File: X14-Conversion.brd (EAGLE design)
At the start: 160 x 100 mm, 34 parts, among them U2 LM2678

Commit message: Added conversion board library
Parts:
- removed +12V, +3.3, 5V, 5V_3.3_TP, GND_TP: TP, TP:TP
- removed +3.3V, +5V, 12V, 5V_3.3, GND, GND3: (no value), SparkFun-Connectors:BANANA_CONN
- removed C14, C29, C30, C31: 10uF, PowerComponents:CTAN(7.30_4.30MM)
- removed C20: 10nF, SparkFun-Capacitors:0603
- removed C24, C25, C26: 150uF, PowerComponents:CTAN(7.30_4.30MM)
- removed C3: 0.47uF, rcl:C0603
- removed D2, D3, D4: (no value), SparkFun-LED:LED-0603
- removed R1, R2, R3, R5: 470, SparkFun-Resistors:0603
- removed R4: 1.2 ohms, SparkFun-Resistors:0603
- removed U$13: 47 uF, Nordic_nRF:RESC0603_N
- removed U$3: SWITCHMODE_SCHOTTKY, PowerComponents:DPAK-3
- removed U$4: TO-263, TPS758:TO-263
- removed U$7: HCM1305, HCM1305:HCM1305
- removed U2: LM2678, PowerComponents:LM2678
- added CB: 10nF 0Ohm, CGA4C2C0G1H103J060AA:CAP_2012_TDK
- added CIN: 120uF 25mOhm, 20SVPF120M:PCAP_SVP_C6_PAN
- added CINX: 100nF 1mOhm, GRM155R71C104KA88D:CAP_GRM_155_MUR
- added COUT: 180uF 30mOhm, 16SVP180MX:CAP_16SVP180MX
- added L1: 15uH 28.5mOhm, IND, 15uH - hcma1305:HCMA1305
- added RFB1: 1kOhm, CRCW04021K00FKED:RES_CRCW_0402
- added RFB2: 3.32kOhm, CRCW04023K32FKED:RES_CRCW_0402
- added U1: LM2678, LM2678SX-ADJNOPB:TS7B
- D1: value (none) -> 550mV 5A; device SparkFun-LED:LED-0603 -> CDBC520-G_Library:CDBC-G
- moved D1 205.8 mm to (-25.4, -5.08)
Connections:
- removed net +12V: +12V.P$1, 12V.P$1, C14.+, C29.+, C3.1, C30.+, C31.+, R5.2, U2.2
- removed net +3.3V: +3.3.P$1, +3.3V.P$1, R3.2, U$13.1, U$4.P$4
- removed net +5V: +5V.P$1, 5V.P$1, R2.2
- removed net +5V_3.3V: 5V_3.3.P$1, 5V_3.3_TP.P$1, C24.+, C25.+, C26.+, R1.2, U$4.P$1, U$4.P$2, U$7.2, U2.6
- removed net GND: C14.-, C24.-, C25.-, C26.-, C29.-, C3.2, C30.-, C31.-, D1.C, D2.C, D3.C, D4.C, GND.P$1, GND3.P$1, GND_TP.P$1, R4.1, U$3.P$1, U$3.P$3, U$4.P$3, U$4.P$6, U2.4, U2.TAB
- removed net N$10: R4.2, U$13.2
- removed net N$2: C20.1, U2.3
- removed net N$4: D2.A, R5.1
- removed net N$5: D3.A, R3.1
- removed net N$6: D4.A, R1.1
- removed net N$7: C20.2, U$3.P$4, U$7.1, U2.1
- removed net N$8: D1.A, R2.1

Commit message: Update new parts library
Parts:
- CB: value 10nF 0Ohm -> 10nF 0Ω
- CIN: value 120uF 25mOhm -> 120uF 25mΩ
- CINX: value 100nF 1mOhm -> 100nF 1mΩ
- COUT: value 180uF 30mOhm -> 180uF 30mΩ
- L1: value 15uH 28.5mOhm -> 15uH
- RFB1: value 1kOhm -> 1kΩ
- RFB2: value 3.32kOhm -> 3.32kΩ
- moved U1 102.9 mm to (-78.7, -71.1)
- moved RFB1 63.8 mm to (-53.3, -41.9)
- moved CIN 61.2 mm to (-52.1, -54.6)
- moved D1 49.7 mm to (-52.1, -47.0)
- moved CB 48.6 mm to (-53.3, -77.5)
- moved CINX 48.6 mm to (-68.6, -80.0)
- moved L1 48.6 mm to (-49.5, -68.6)
- moved RFB2 48.6 mm to (-53.3, -59.7)
- moved COUT 48.6 mm to (-66.0, -69.8)
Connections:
- new net GND: RFB1.1
- new net N$1: RFB1.2, RFB2.2, U1.6

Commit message: Complete Schematic for LM2678
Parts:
- U1: value LM2678 -> LM2678SX-ADJ/NOPBTS7B
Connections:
- new net 12V: CIN.1, CINX.1, U1.2
- new net 5V: COUT.1, L1.2, RFB2.1
- new net N$2: CB.1, U1.3
- new net N$3: CB.2, D1.1, L1.1, U1.1
- net GND: now also CIN.2, CINX.2, COUT.2, D1.2, U1.4
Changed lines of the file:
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@@
 <attribute name="VALUE" x="-70.3088" y="-80.645" size="1.27" layer="27" ratio="6"/>
 </element>
-<element name="U1" library="LM2678SX-ADJNOPB" package="TS7B" value="LM2678" x="-78.74" y="-71.12" smashed="yes">
+<element name="U1" library="LM2678SX-ADJNOPB" package="TS7B" value="LM2678SX-ADJ/NOPBTS7B" x="-78.74" y="-71.12" smashed="yes">
 <attribute name="COPYRIGHT" value="Copyright (C) 2021 Ultra Librarian. All rights reserved." x="-78.74" y="-71.12" size="1.778" layer="27" display="off"/>
 <attribute name="DIGI-KEY_PART_NUMBER_1" value="LM2678SX-ADJ/NOPBCT-ND" x="-78.74" y="-71.12" size="1.778" layer="27" display="off"/>
@@
 </elements>
 <signals>
-<signal name="GND">
-<contactref element="RFB1" pad="1"/>
-</signal>
 <signal name="N$1">
 <contactref element="U1" pad="6"/>
@@
 <wire x1="-52.8701" y1="-41.91" x2="-52.8701" y2="-59.69" width="0" layer="19" extent="1-1"/>
 </signal>
+<signal name="GND">
+<contactref element="RFB1" pad="1"/>
+<contactref element="COUT" pad="2"/>
+<contactref element="D1" pad="2"/>
+<contactref element="CIN" pad="2"/>
+<contactref element="CINX" pad="2"/>
+<contactref element="U1" pad="4"/>
+<wire x1="-68.0593" y1="-80.01" x2="-78.74" y2="-79.4004" width="0" layer="19" extent="1-1"/>
+<wire x1="-61.69" y1="-69.85" x2="-68.0593" y2="-80.01" width="0" layer="19" extent="1-1"/>
+<wire x1="-49.3141" y1="-54.61" x2="-61.69" y2="-69.85" width="0" layer="19" extent="1-1"/>
+<wire x1="-48.943" y1="-46.99" x2="-49.3141" y2="-54.61" width="0" layer="19" extent="1-1"/>
+<wire x1="-53.8099" y1="-41.91" x2="-48.943" y2="-46.99" width="0" layer="19" extent="1-1"/>
+</signal>
+<signal name="N$2">
+<contactref element="U1" pad="3"/>
+<contactref element="CB" pad="1"/>
+<wire x1="-54.5211" y1="-77.47" x2="-80.01" y2="-79.4004" width="0" layer="19" extent="1-1"/>
+</signal>
+<signal name="N$3">
+<contactref element="U1" pad="1"/>
+<contactref element="L1" pad="1"/>
+<contactref element="CB" pad="2"/>
+<contactref element="D1" pad="1"/>
+<wire x1="-55.13" y1="-68.58" x2="-82.55" y2="-79.4004" width="0" layer="19" extent="1-1"/>
+<wire x1="-52.1589" y1="-77.47" x2="-55.13" y2="-68.58" width="0" layer="19" extent="1-1"/>
+<wire x1="-55.197" y1="-46.99" x2="-55.13" y2="-68.58" width="0" layer="19" extent="1-1"/>
+</signal>
+<signal name="12V">
+<contactref element="U1" pad="2"/>
+<contactref element="CIN" pad="1"/>
+<contactref element="CINX" pad="1"/>
+<wire x1="-69.1007" y1="-80.01" x2="-81.28" y2="-79.4004" width="0" layer="19" extent="1-1"/>
+<wire x1="-54.8259" y1="-54.61" x2="-69.1007" y2="-80.01" width="0" layer="19" extent="1-1"/>
+</signal>
+<signal name="5V">
+<contactref element="L1" pad="2"/>
+<contactref element="COUT" pad="1"/>
+<contactref element="RFB2" pad="1"/>
+<wire x1="-53.8099" y1="-59.69" x2="-70.39" y2="-69.85" width="0" layer="19" extent="1-1"/>
+<wire x1="-43.93" y1="-68.58" x2="-53.8099" y2="-59.69" width="0" layer="19" extent="1-1"/>
+</signal>
 </signals>

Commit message: Fix Schematic
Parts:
- added C1: 10uF 16V, CAP_GRM21BR61C106KE15L:CAPC2012X135N
- added C2: 22uF 16V, CAP_GRM21BR61C226ME44L:CAPC2012X145N
- added U$1: SOT150P410X160-3N, AZ1117C-3.3:SOT150P410X160-3N
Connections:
- new net 3.3V: C1.1, U$1.2
- net 5V: now also C2.1, U$1.3
- net GND: now also C1.2, C2.2, U$1.1
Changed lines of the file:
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@@
 <attribute name="VALUE" x="-80.4688" y="-71.755" size="1.27" layer="27" ratio="6"/>
+</element>
+<element name="U$1" library="AZ1117C-3.3" package="SOT150P410X160-3N" value="SOT150P410X160-3N" x="-74.93" y="-90.17" smashed="yes">
+<attribute name="NAME" x="-82.601959375" y="-85.967259375" size="3.2051" layer="25" display="off"/>
+<attribute name="VALUE" x="-83.074790625" y="-95.6813" size="1.27" layer="27"/>
+</element>
+<element name="C1" library="CAP_GRM21BR61C106KE15L" package="CAPC2012X135N" value="10uF 16V" x="-82.55" y="-99.06" smashed="yes">
+<attribute name="DESCRIPTION" value=" 10 µF ±10% 16V Ceramic Capacitor X5R 0805 (2012 Metric) " x="-82.55" y="-99.06" size="1.778" layer="27" display="off"/>
+<attribute name="DIGI-KEY_PART_NUMBER" value="490-3886-2-ND" x="-82.55" y="-99.06" size="1.778" layer="27" display="off"/>
+<attribute name="MF" value="Murata" x="-82.55" y="-99.06" size="1.778" layer="27" display="off"/>
+<attribute name="MP" value="GRM21BR61C106KE15L" x="-82.55" y="-99.06" size="1.778" layer="27" display="off"/>
+<attribute name="NAME" x="-84.21" y="-98.04" size="0.5" layer="25"/>
+<attribute name="PACKAGE" value="2012 Murata" x="-82.55" y="-99.06" size="1.778" layer="27" display="off"/>
+<attribute name="PURCHASE-URL" value="https://pricing.snapeda.com/search/part/GRM21BR61C106KE15L/?ref=eda" x="-82.55" y="-99.06" size="1.778" layer="27" display="off"/>
+<attribute name="VALUE" x="-84.21" y="-100.08" size="0.5" layer="27" align="top-left"/>
+</element>
+<element name="C2" library="CAP_GRM21BR61C226ME44L" package="CAPC2012X145N" value="22uF 16V" x="-82.55" y="-102.87" smashed="yes">
+<attribute name="DESCRIPTION" value=" SMD Capacitor X5R(EIA) with Capacitance: 22uF Tol. 20%. Rated Voltage: 16Vdc " x="-82.55" y="-102.87" size="1.778" layer="27" display="off"/>
+<attribute name="DIGI-KEY_PART_NUMBER" value="490-10747-2-ND" x="-82.55" y="-102.87" size="1.778" layer="27" display="off"/>
+<attribute name="MF" value="Murata" x="-82.55" y="-102.87" size="1.778" layer="27" display="off"/>
+<attribute name="MP" value="GRM21BR61C226ME44L" x="-82.55" y="-102.87" size="1.778" layer="27" display="off"/>
+<attribute name="NAME" x="-84.26" y="-101.8" size="0.5" layer="25"/>
+<attribute name="PACKAGE" value="2012 Murata" x="-82.55" y="-102.87" size="1.778" layer="27" display="off"/>
+<attribute name="PURCHASE-URL" value="https://pricing.snapeda.com/search/part/GRM21BR61C226ME44L/?ref=eda" x="-82.55" y="-102.87" size="1.778" layer="27" display="off"/>
+<attribute name="VALUE" x="-84.26" y="-103.94" size="0.5" layer="27" align="top-left"/>
 </element>
 </elements>
@@
 <contactref element="CINX" pad="2"/>
 <contactref element="U1" pad="4"/>
+<contactref element="C2" pad="2"/>
+<contactref element="U$1" pad="1"/>
+<contactref element="C1" pad="2"/>
+<wire x1="-81.662" y1="-99.06" x2="-81.65" y2="-102.87" width="0" layer="19" extent="1-1"/>
+<wire x1="-76.429" y1="-92.151" x2="-81.662" y2="-99.06" width="0" layer="19" extent="1-1"/>
+<wire x1="-78.74" y1="-79.4004" x2="-76.429" y2="-92.151" width="0" layer="19" extent="1-1"/>
 <wire x1="-68.0593" y1="-80.01" x2="-78.74" y2="-79.4004" width="0" layer="19" extent="1-1"/>
 <wire x1="-61.69" y1="-69.85" x2="-68.0593" y2="-80.01" width="0" layer="19" extent="1-1"/>
@@
 <contactref element="COUT" pad="1"/>
 <contactref element="RFB2" pad="1"/>
+<contactref element="U$1" pad="3"/>
+<contactref element="C2" pad="1"/>
+<wire x1="-73.431" y1="-92.151" x2="-83.45" y2="-102.87" width="0" layer="19" extent="1-1"/>
+<wire x1="-70.39" y1="-69.85" x2="-73.431" y2="-92.151" width="0" layer="19" extent="1-1"/>
 <wire x1="-53.8099" y1="-59.69" x2="-70.39" y2="-69.85" width="0" layer="19" extent="1-1"/>
 <wire x1="-43.93" y1="-68.58" x2="-53.8099" y2="-59.69" width="0" layer="19" extent="1-1"/>
 </signal>
+<signal name="3.3V">
+<contactref element="U$1" pad="2"/>
+<contactref element="C1" pad="1"/>
+<wire x1="-74.93" y1="-91.897" x2="-83.438" y2="-99.06" width="0" layer="19" extent="1-1"/>
+</signal>
 </signals>

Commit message: Completing Schematic
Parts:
- added CONN: DISTRIBUTION-CONVERSION, CONN, Distribution-Conversion:TSW-105-05-G-S
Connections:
- new net 5.2V: C2.1, COUT.1, L1.2, RFB2.1, U$1.3
- net 12V: now also CONN.1
- net 3.3V: now also CONN.2
- net 5V: now also CONN.3; no longer C2.1, COUT.1, L1.2, RFB2.1, U$1.3
- net GND: now also CONN.4, CONN.5
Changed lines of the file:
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@@
 <attribute name="VALUE" x="-84.26" y="-103.94" size="0.5" layer="27" align="top-left"/>
+</element>
+<element name="CONN" library="CONN, Distribution-Conversion" package="TSW-105-05-G-S" value="DISTRIBUTION-CONVERSION" x="-77.47" y="-109.22" smashed="yes">
+<attribute name="NAME" x="-83.82" y="-107.95" size="1.778" layer="25"/>
 </element>
 </elements>
@@
 <contactref element="U$1" pad="1"/>
 <contactref element="C1" pad="2"/>
+<contactref element="CONN" pad="5"/>
+<contactref element="CONN" pad="4"/>
 <wire x1="-81.662" y1="-99.06" x2="-81.65" y2="-102.87" width="0" layer="19" extent="1-1"/>
 <wire x1="-76.429" y1="-92.151" x2="-81.662" y2="-99.06" width="0" layer="19" extent="1-1"/>
+<wire x1="-74.95" y1="-109.22" x2="-81.65" y2="-102.87" width="0" layer="19" extent="1-1"/>
+<wire x1="-72.41" y1="-109.22" x2="-74.95" y2="-109.22" width="0" layer="19" extent="1-1"/>
 <wire x1="-78.74" y1="-79.4004" x2="-76.429" y2="-92.151" width="0" layer="19" extent="1-1"/>
 <wire x1="-68.0593" y1="-80.01" x2="-78.74" y2="-79.4004" width="0" layer="19" extent="1-1"/>
@@
 <wire x1="-55.197" y1="-46.99" x2="-55.13" y2="-68.58" width="0" layer="19" extent="1-1"/>
 </signal>
-<signal name="12V">
-<contactref element="U1" pad="2"/>
-<contactref element="CIN" pad="1"/>
-<contactref element="CINX" pad="1"/>
-<wire x1="-69.1007" y1="-80.01" x2="-81.28" y2="-79.4004" width="0" layer="19" extent="1-1"/>
-<wire x1="-54.8259" y1="-54.61" x2="-69.1007" y2="-80.01" width="0" layer="19" extent="1-1"/>
+<signal name="5V">
+<contactref element="CONN" pad="3"/>
 </signal>
-<signal name="5V">
+<signal name="3.3V">
+<contactref element="U$1" pad="2"/>
+<contactref element="C1" pad="1"/>
+<contactref element="CONN" pad="2"/>
+<wire x1="-83.438" y1="-99.06" x2="-80.03" y2="-109.22" width="0" layer="19" extent="1-1"/>
+<wire x1="-74.93" y1="-91.897" x2="-83.438" y2="-99.06" width="0" layer="19" extent="1-1"/>
+</signal>
+<signal name="5.2V">
 <contactref element="L1" pad="2"/>
 <contactref element="COUT" pad="1"/>
@@
 <wire x1="-43.93" y1="-68.58" x2="-53.8099" y2="-59.69" width="0" layer="19" extent="1-1"/>
 </signal>
-<signal name="3.3V">
-<contactref element="U$1" pad="2"/>
-<contactref element="C1" pad="1"/>
-<wire x1="-74.93" y1="-91.897" x2="-83.438" y2="-99.06" width="0" layer="19" extent="1-1"/>
+<signal name="12V">
+<contactref element="U1" pad="2"/>
+<contactref element="CIN" pad="1"/>
+<contactref element="CINX" pad="1"/>
+<contactref element="CONN" pad="1"/>
+<wire x1="-81.28" y1="-79.4004" x2="-82.57" y2="-109.22" width="0" layer="19" extent="1-1"/>
+<wire x1="-69.1007" y1="-80.01" x2="-81.28" y2="-79.4004" width="0" layer="19" extent="1-1"/>
+<wire x1="-54.8259" y1="-54.61" x2="-69.1007" y2="-80.01" width="0" layer="19" extent="1-1"/>
 </signal>
 </signals>

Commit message: Completing Schematic (1) and Upload Datasheets
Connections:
- removed net 5V: CONN.3
- net 5.2V: now also CONN.3
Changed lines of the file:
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@@
 <wire x1="-55.197" y1="-46.99" x2="-55.13" y2="-68.58" width="0" layer="19" extent="1-1"/>
-</signal>
-<signal name="5V">
-<contactref element="CONN" pad="3"/>
 </signal>
 <signal name="3.3V">
@@
 <contactref element="U$1" pad="3"/>
 <contactref element="C2" pad="1"/>
+<contactref element="CONN" pad="3"/>
+<wire x1="-83.45" y1="-102.87" x2="-77.49" y2="-109.22" width="0" layer="19" extent="1-1"/>
 <wire x1="-73.431" y1="-92.151" x2="-83.45" y2="-102.87" width="0" layer="19" extent="1-1"/>
 <wire x1="-70.39" y1="-69.85" x2="-73.431" y2="-92.151" width="0" layer="19" extent="1-1"/>

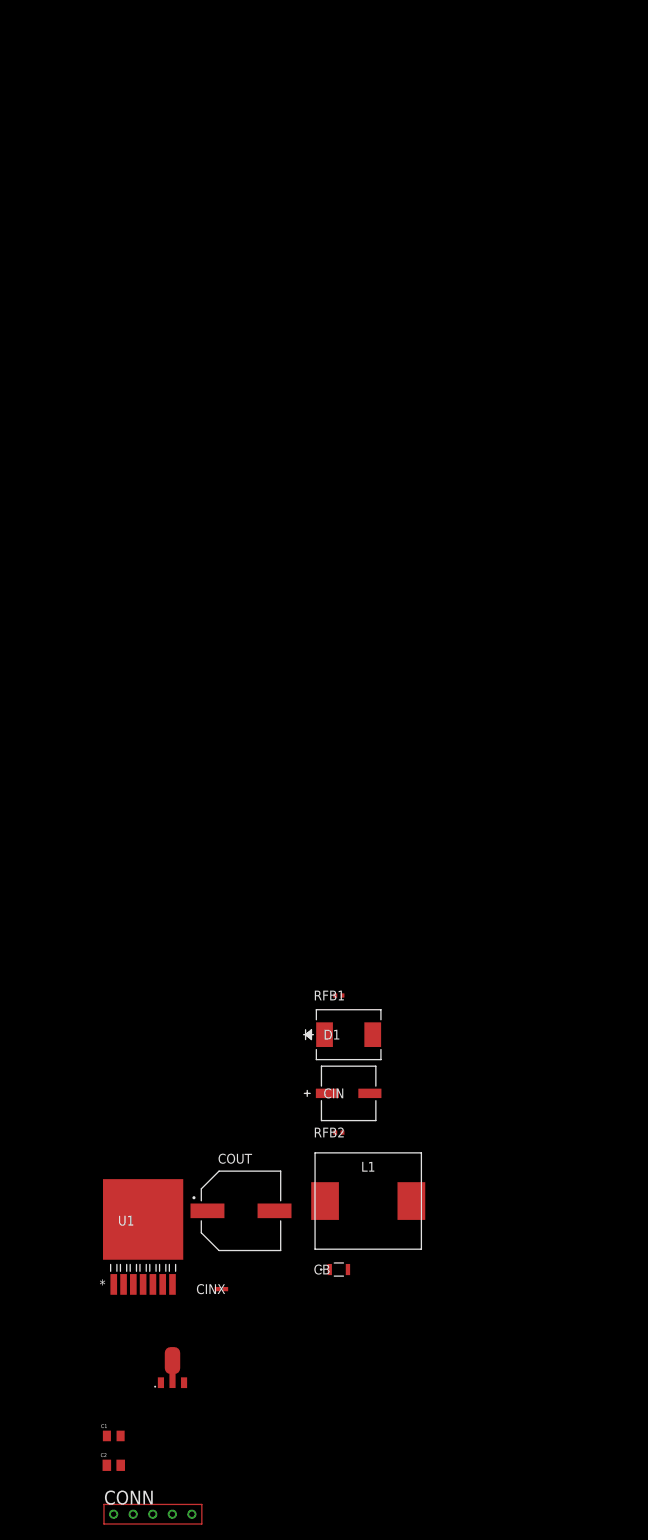
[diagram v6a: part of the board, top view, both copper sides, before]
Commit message: Fix Schematic, add test points, screw terminals and connectors
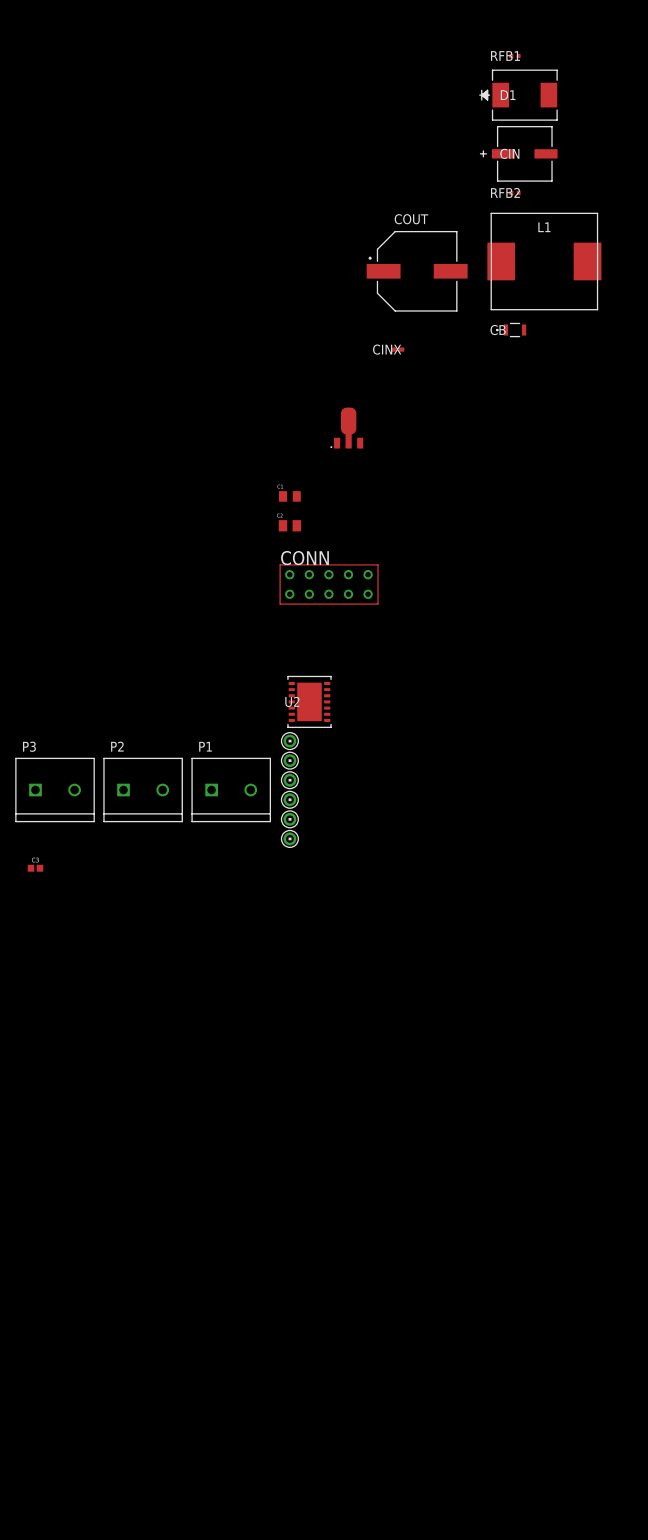
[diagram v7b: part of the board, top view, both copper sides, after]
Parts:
- removed U1: LM2678SX-ADJ/NOPBTS7B, LM2678SX-ADJNOPB:TS7B
- added C3: 0.1uF, SparkFun-Capacitors:0402
- added P1, P2, P3: 282837-2, ScrewPoints_282837-2:TE_282837-2
- added U$2: 3.3V_TESTPOINT, testpoints:3.3V_TESTPOINT
- added U$3: 5.2V_TESTPOINT, testpoints:5.2V_TESTPOINT
- added U$4: 12V_TESTPOINT, testpoints:12V_TESTPOINT
- added U$5, U$6, U$7: GND_TESTPOINT, testpoints:GND_TESTPOINT
- added U2: LM2678SD-ADJ/NOPB, LM2678SX-ADJNOPB:SRC14A
- moved D1 124.0 mm to (-29.2, 74.9)
- moved C1 124.0 mm to (-59.7, 22.9)
- moved C2 124.0 mm to (-59.7, 19.1)
- moved CB 124.0 mm to (-30.5, 44.5)
- moved CIN 124.0 mm to (-29.2, 67.3)
- moved CINX 124.0 mm to (-45.7, 41.9)
- moved CONN 124.0 mm to (-54.6, 12.7)
- moved L1 124.0 mm to (-26.7, 53.3)
- moved RFB1 124.0 mm to (-30.5, 80.0)
- moved U$1 124.0 mm to (-52.1, 31.8)
- moved COUT 124.0 mm to (-43.2, 52.1)
- moved RFB2 124.0 mm to (-30.5, 62.2)
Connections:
- removed net N$1: RFB1.2, RFB2.2, U1.6
- removed net N$3: CB.2, D1.1, L1.1, U1.1
- new net N$4: CB.1, U2.4
- new net N$5: RFB1.2, RFB2.2, U2.7
- net 12V: now also CONN.6, P2.2, U$4.12V, U2.3; no longer U1.2
- net 3.3V: now also CONN.7, P1.2, U$2.3.3V
- net 5.2V: now also C3.1, CONN.8, P1.1, U$3.5.2V
- net GND: now also C3.2, CONN.10, CONN.9, P2.1, P3.1, P3.2, U$5.GND, U$6.GND, U$7.GND, U2.15, U2.9; no longer U1.4
- net N$2: now also CB.2, D1.1, L1.1, U2.14; no longer CB.1, U1.3
